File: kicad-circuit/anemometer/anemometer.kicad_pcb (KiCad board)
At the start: 2 copper layers, 152.4 x 76.2 mm, 55 parts, among them J5VIN1 Conn_01x03, J5VIN2 Conn_01x03, Q1 TIP41, Q2 2N3906, U1 LM358, U2 LM324

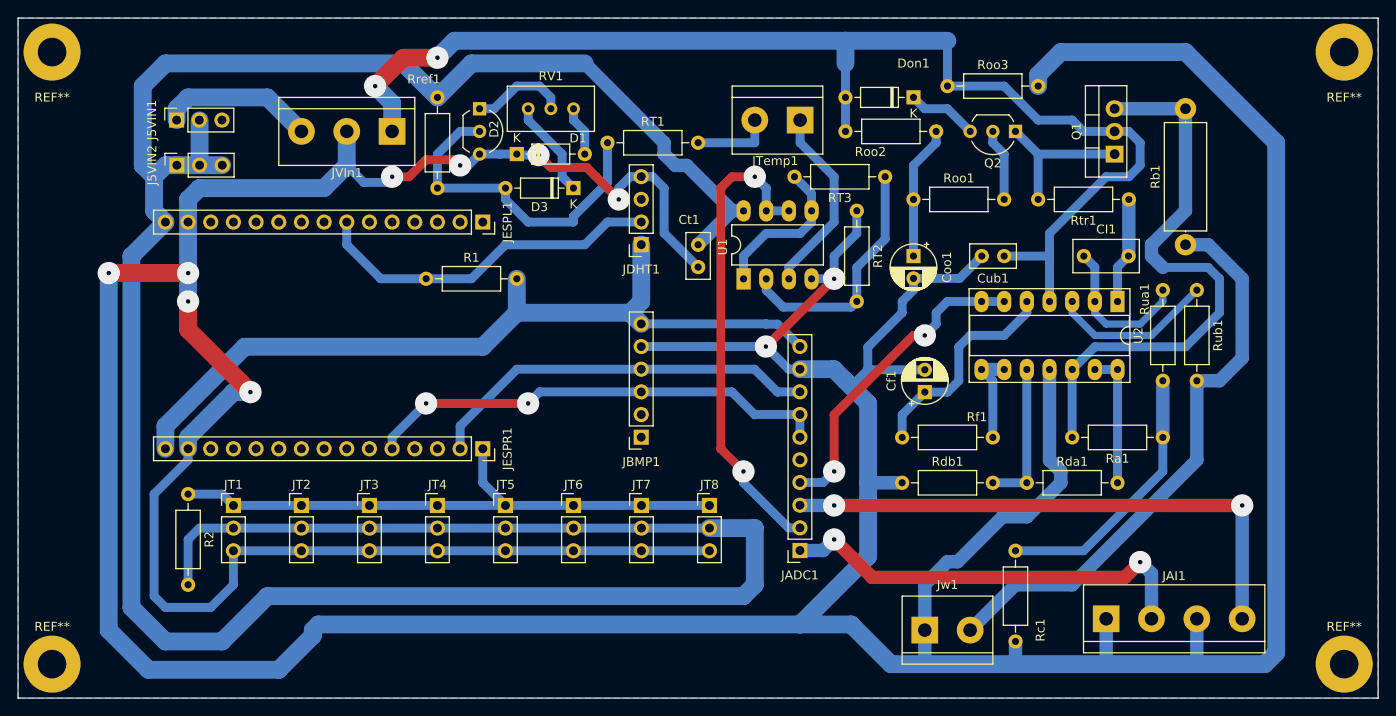
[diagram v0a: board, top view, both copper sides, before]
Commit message: Changed a little bit the tracks on the upper side
Since I will be building the boards by hand, the upper side tracks should no pass under resistors and other components so I rearranged a few things.
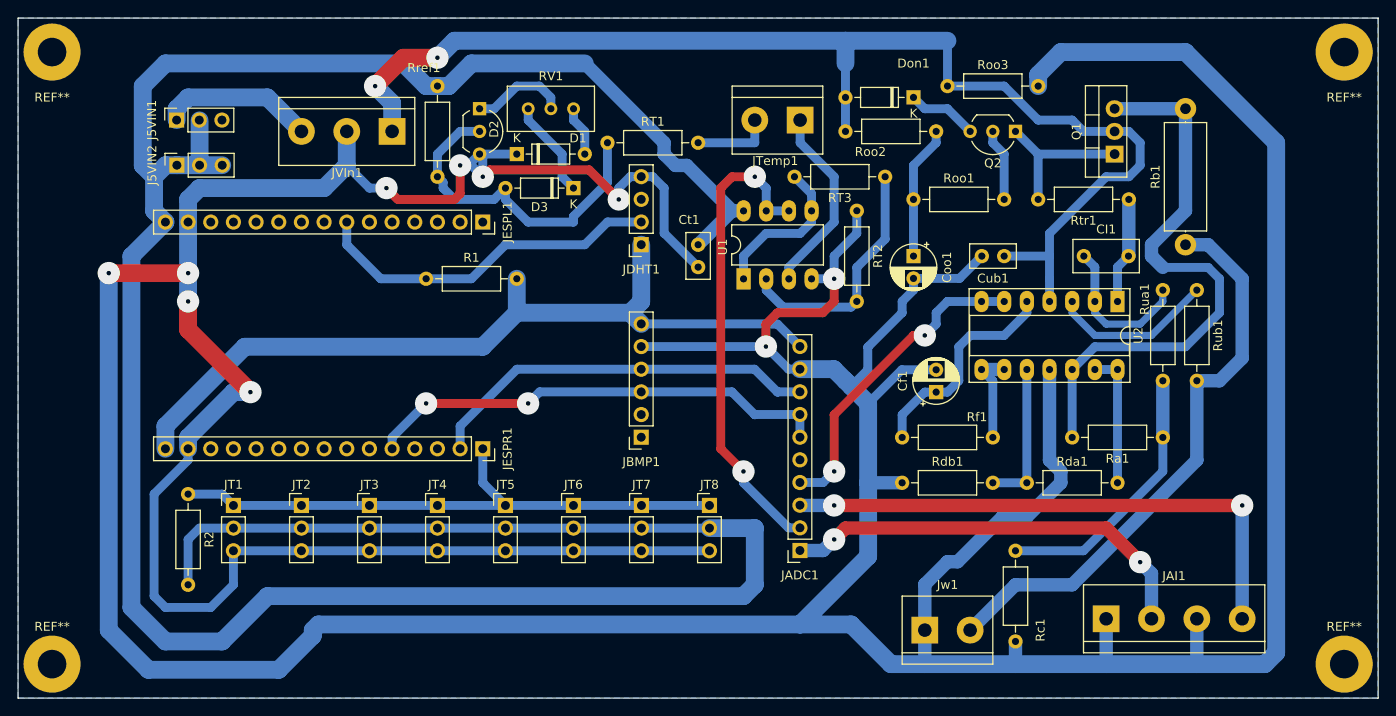
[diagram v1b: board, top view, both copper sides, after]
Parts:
- moved Rref1 1.27 mm to (123.2, 45.7)
- moved Cf1 1.27 mm to (179.1, 80.0)
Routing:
- net GND: track 640.2 -> 658.2 mm
- net /5V: track 308.4 -> 307.3 mm
- net /Vref: track 37.6 -> 38.3 mm

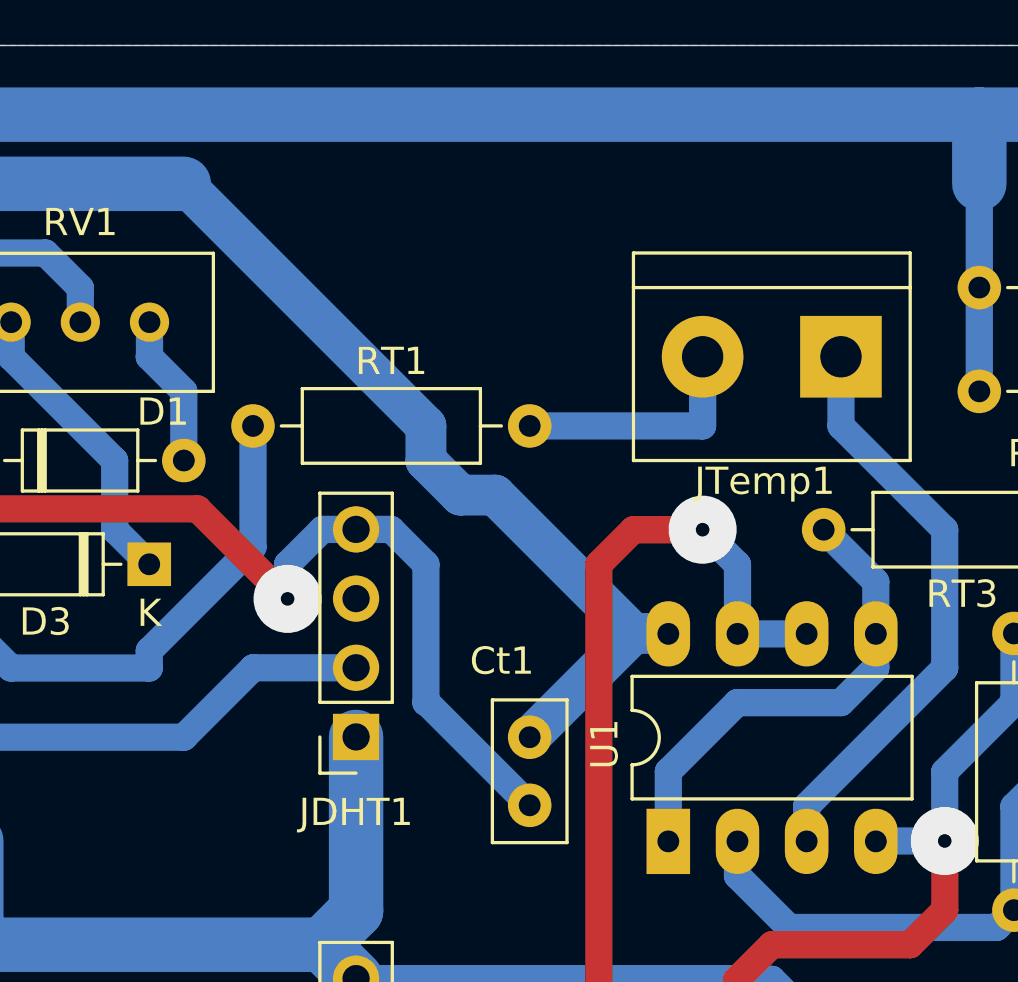
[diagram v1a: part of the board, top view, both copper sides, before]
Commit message: Corrected the thermistor temperature circuit.
There was a mistake. I corrected it ion the board that I built and now it is corrected in the Kicad circuit.
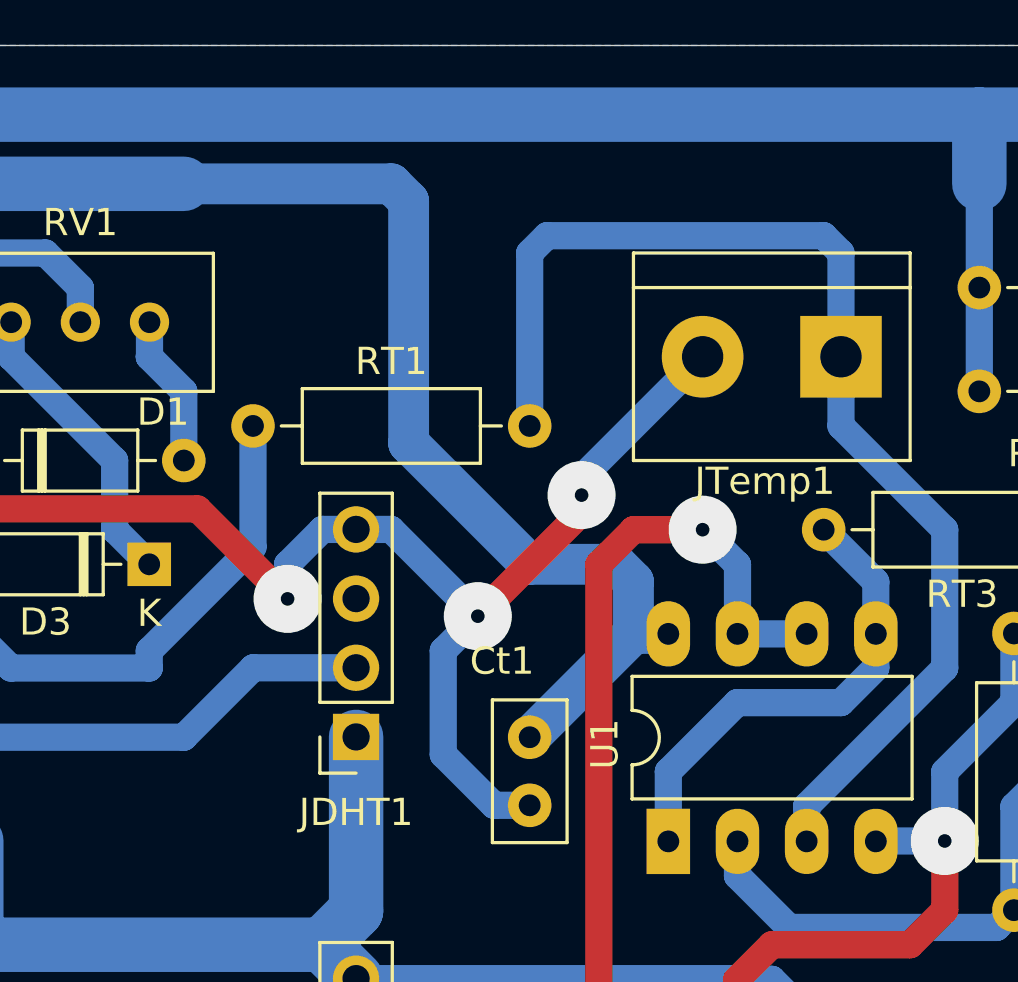
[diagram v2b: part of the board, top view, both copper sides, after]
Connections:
- JTemp1 pad 1: Net-(JTemp1-Pad1) -> Net-(RT1-Pad2)
- JTemp1 pad 2: Net-(JTemp1-Pad2) -> GND
- RT1 pad 2: Net-(JTemp1-Pad2) -> Net-(RT1-Pad2)
- U1 pad 3: Net-(JTemp1-Pad1) -> Net-(RT1-Pad2)
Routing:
- net Net-(RT1-Pad2): track 0.00 -> 43.6 mm
- net Net-(JTemp1-Pad1): track 21.5 -> 0.00 mm
- net GND: track 658.2 -> 672.9 mm, vias 10 -> 12
- net Net-(JTemp1-Pad2): track 8.89 -> 0.00 mm
- net /5V: track 307.3 -> 312.9 mm

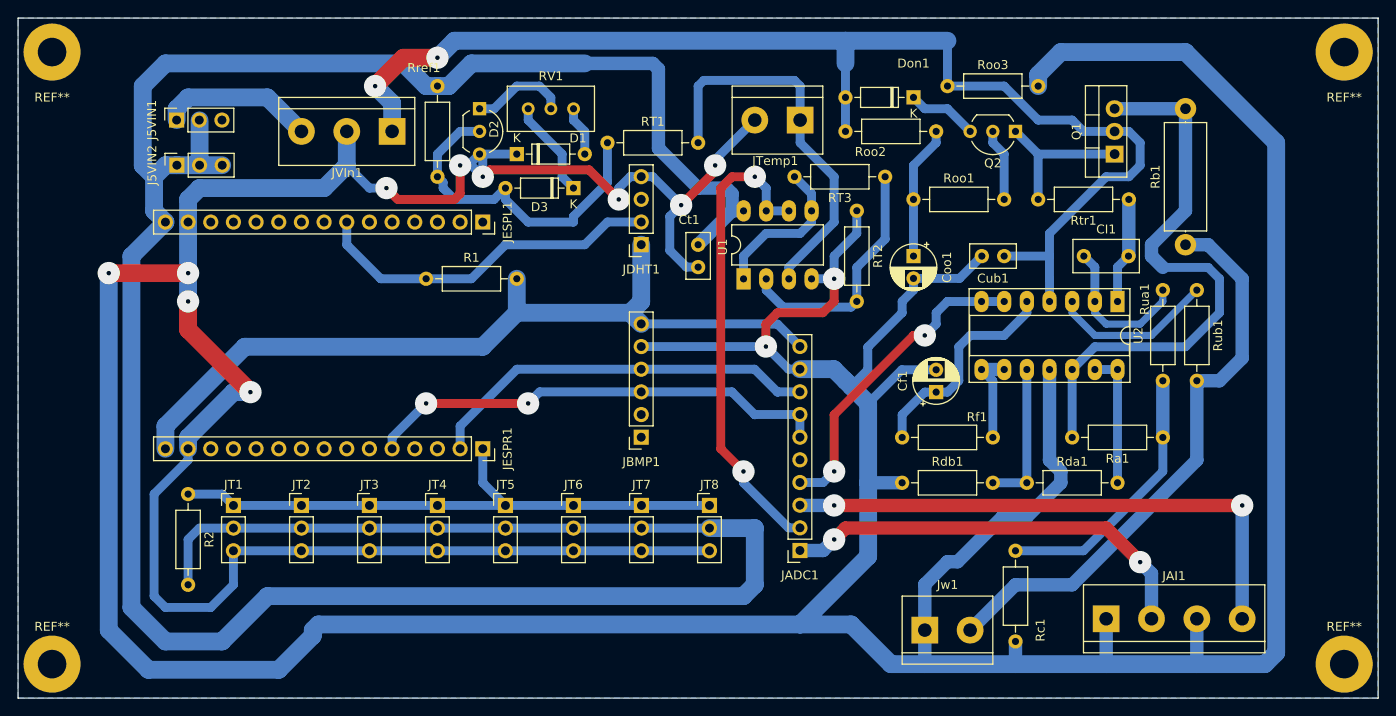
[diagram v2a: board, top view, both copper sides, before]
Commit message: Switched pins of DS18B20 temp. sensor
Now the tracks are positioned in the same orientation as the pins in the TO-92 packaging. Not important but now I can solder one sensor directly on the board.
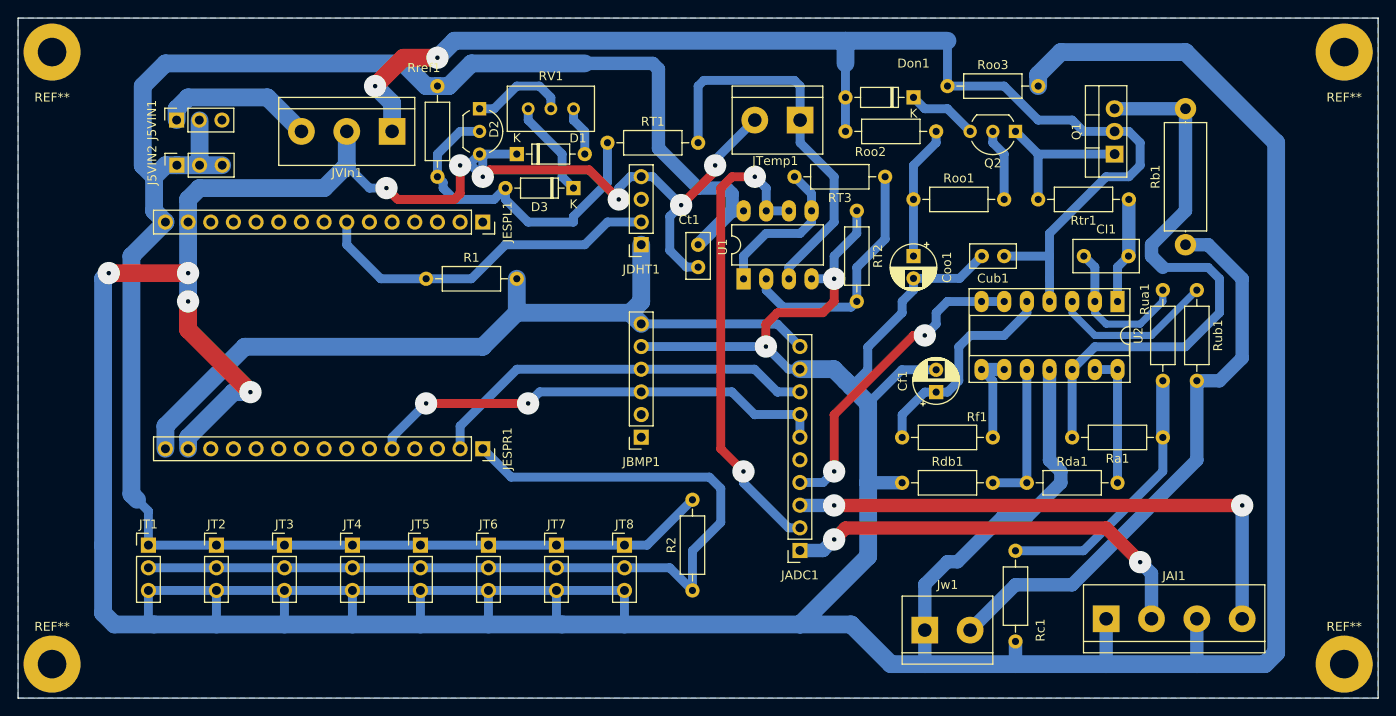
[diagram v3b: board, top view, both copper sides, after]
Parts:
- moved R2 57.5 mm to (151.8, 102.2), turned to 90 degrees
- moved JT2 10.5 mm to (98.4, 97.2)
- moved JT5 10.5 mm to (121.3, 97.2)
- moved JT6 10.5 mm to (128.9, 97.2)
- moved JT7 10.5 mm to (136.5, 97.2)
- moved JT1 10.5 mm to (90.8, 97.2)
- moved JT3 10.5 mm to (106.0, 97.2)
- moved JT4 10.5 mm to (113.7, 97.2)
- moved JT8 10.5 mm to (144.1, 97.2)
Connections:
- JESPR1 pad 1: Net-(JESPR1-Pad1) -> Net-(JT2-Pad2)
- JT1 pad 1: Net-(JESPR1-Pad1) -> /5V
- JT1 pad 2: /5V -> Net-(JT2-Pad2)
- JT2 pad 1: Net-(JESPR1-Pad1) -> /5V
- JT2 pad 2: /5V -> Net-(JT2-Pad2)
- JT3 pad 1: Net-(JESPR1-Pad1) -> /5V
- JT3 pad 2: /5V -> Net-(JT2-Pad2)
- JT4 pad 1: Net-(JESPR1-Pad1) -> /5V
- JT4 pad 2: /5V -> Net-(JT2-Pad2)
- JT5 pad 1: Net-(JESPR1-Pad1) -> /5V
- JT5 pad 2: /5V -> Net-(JT2-Pad2)
- JT6 pad 1: Net-(JESPR1-Pad1) -> /5V
- JT6 pad 2: /5V -> Net-(JT2-Pad2)
- JT7 pad 1: Net-(JESPR1-Pad1) -> /5V
- JT7 pad 2: /5V -> Net-(JT2-Pad2)
- JT8 pad 1: Net-(JESPR1-Pad1) -> /5V
- JT8 pad 2: /5V -> Net-(JT2-Pad2)
- R2 pad 1: Net-(JESPR1-Pad1) -> Net-(JT2-Pad2)
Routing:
- net Net-(JT2-Pad2): track 0.00 -> 103.3 mm
- net /5V: track 312.9 -> 220.2 mm
- net Net-(JESPR1-Pad1): track 66.3 -> 0.00 mm
- net GND: track 672.9 -> 666.7 mm

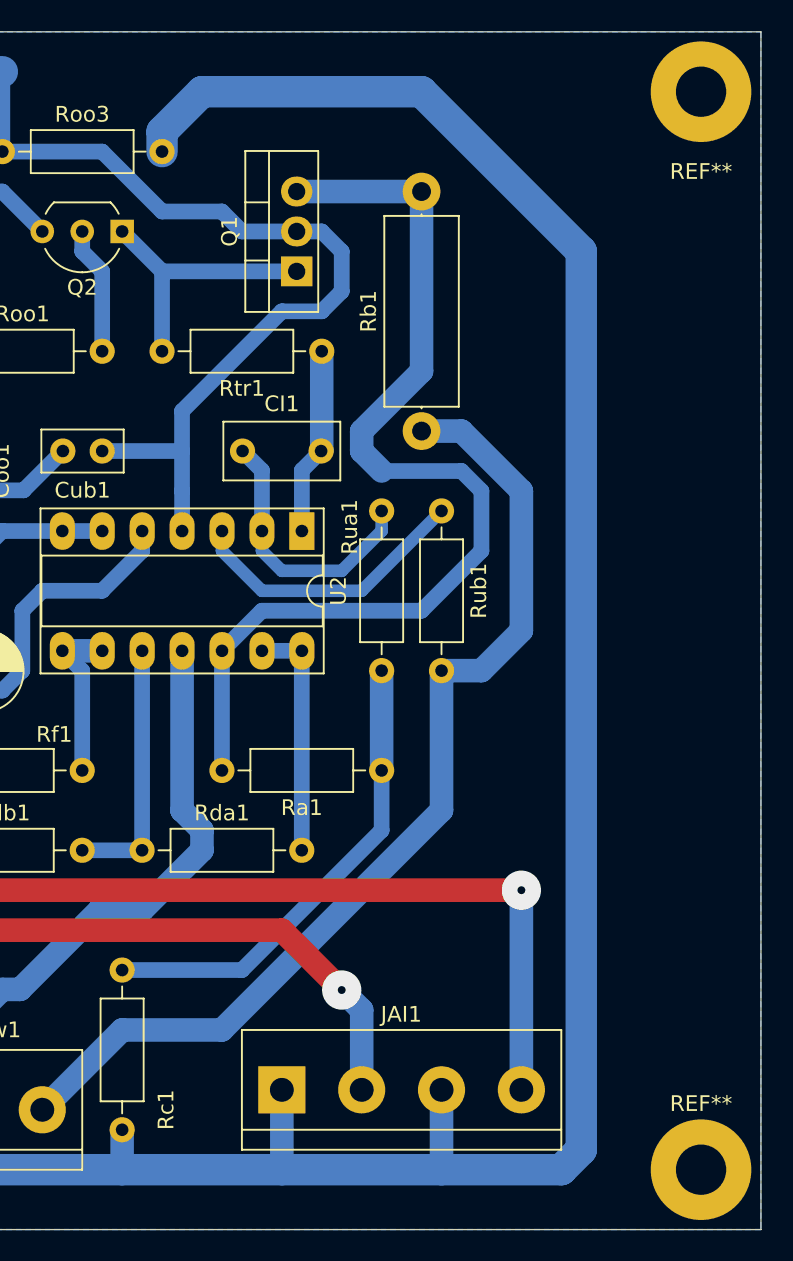
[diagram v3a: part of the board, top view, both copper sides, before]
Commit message: Moved some components so that the TIP41 transistor can lay on its back
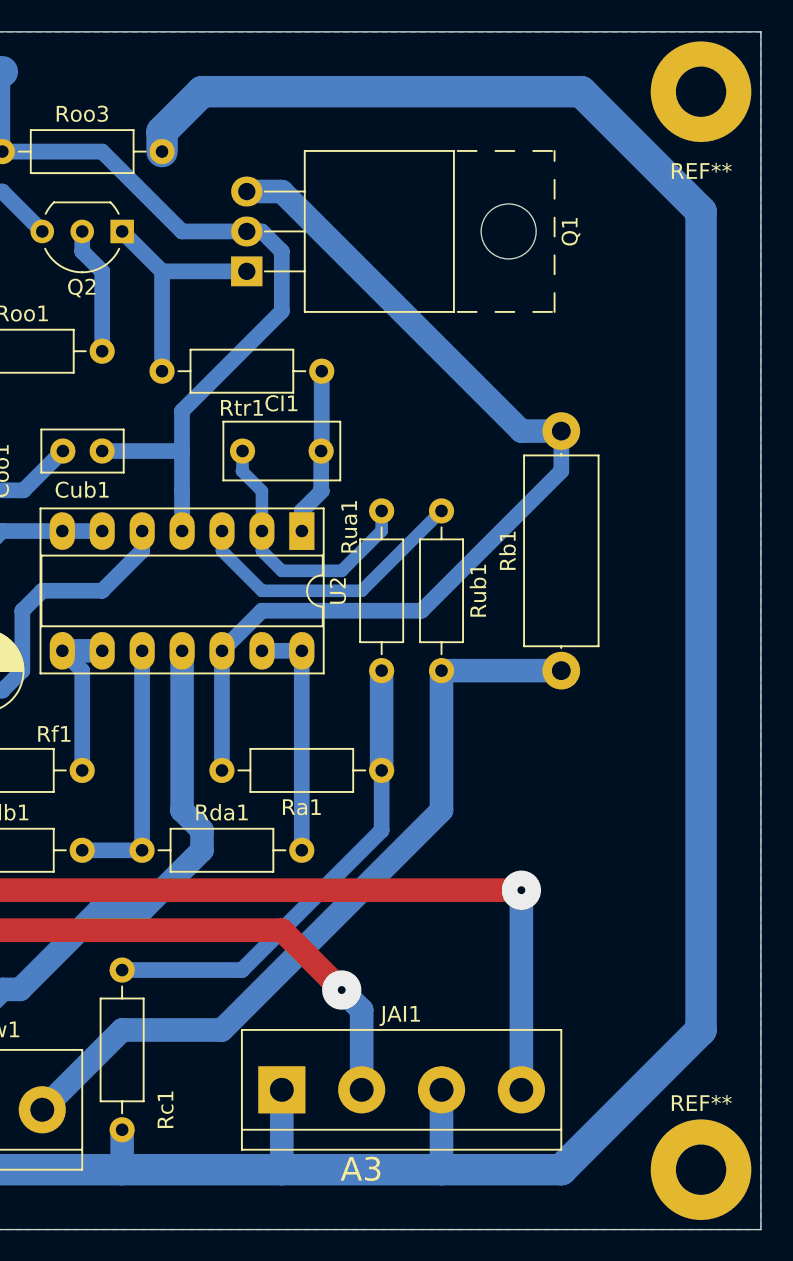
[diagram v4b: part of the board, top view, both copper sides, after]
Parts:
- Q1: footprint Package_TO_SOT_THT:TO-220-3_Vertical -> Package_TO_SOT_THT:TO-220-3_Horizontal_TabUp
- moved Rb1 17.6 mm to (215.9, 78.7)
- moved Q1 3.18 mm to (195.9, 53.3)
- moved Rtr1 1.27 mm to (200.7, 59.7)
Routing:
- net Net-(Jw1-Pad2): track 65.1 -> 49.8 mm
- net GND: track 666.7 -> 679.0 mm
- net VCC: track 140.1 -> 133.3 mm
- net /Vwo: track 65.3 -> 62.8 mm
- net /Von: track 17.2 -> 15.3 mm
- net Net-(CI1-Pad2): track 12.0 -> 10.7 mm
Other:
- board text added: "A3"
